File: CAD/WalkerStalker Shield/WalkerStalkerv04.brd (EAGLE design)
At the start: 49.5 x 53.3 mm, 25 parts

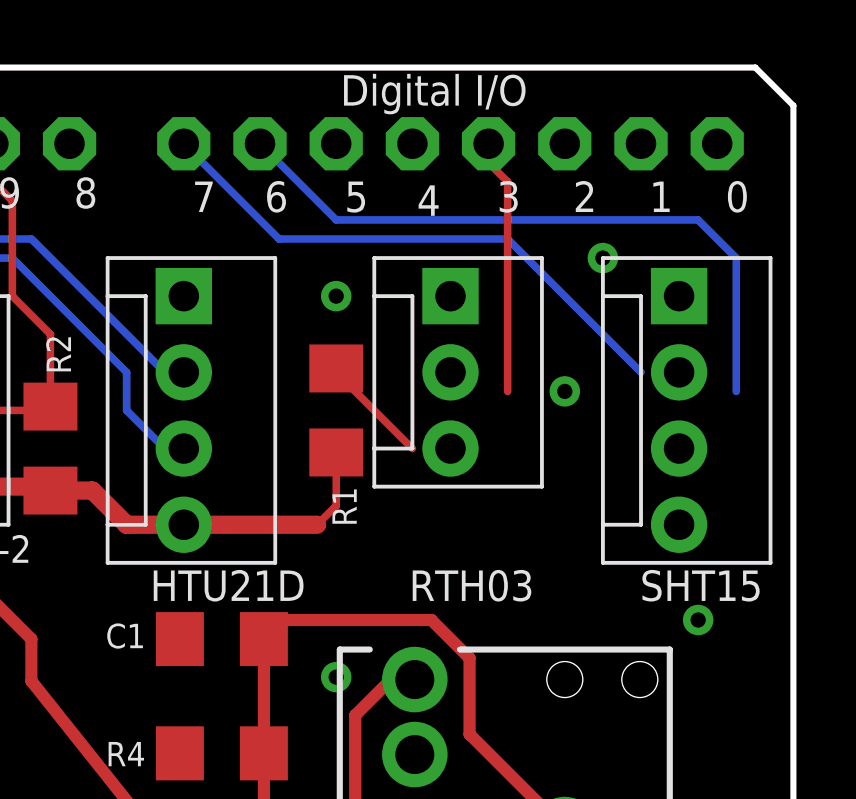
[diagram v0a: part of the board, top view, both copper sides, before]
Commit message: Fixed Temperature sensors
+ Temperature sensors are now called by explicit address, rather than
index, which was not consistent (could not tell if sensor was wall or
air)
+ Unit IDs are not transmitted in data packets for easy identification
+Mounting bracket for TMP006 sensor added (3D file)
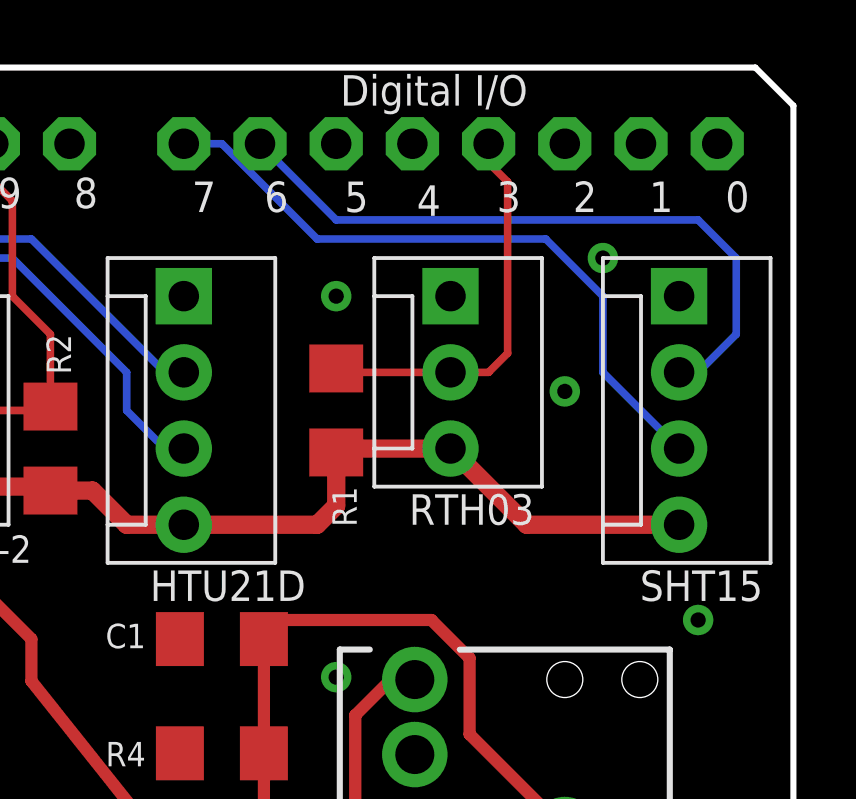
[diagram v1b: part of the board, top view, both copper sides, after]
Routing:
- net +3V3: track 119.1 -> 132.4 mm
- net SHT15-CL: track 18.4 -> 22.2 mm
- net RHT03: track 12.2 -> 13.4 mm
- net SHT15-DA: track 21.9 -> 22.4 mm
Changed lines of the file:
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@@
 <layer number="23" name="tOrigins" color="15" fill="1" visible="yes" active="yes"/>
 <layer number="24" name="bOrigins" color="15" fill="1" visible="yes" active="yes"/>
-<layer number="25" name="tNames" color="7" fill="1" visible="no" active="yes"/>
+<layer number="25" name="tNames" color="7" fill="1" visible="yes" active="yes"/>
 <layer number="26" name="bNames" color="7" fill="1" visible="no" active="yes"/>
-<layer number="27" name="tValues" color="7" fill="1" visible="no" active="yes"/>
+<layer number="27" name="tValues" color="7" fill="1" visible="yes" active="yes"/>
 <layer number="28" name="bValues" color="7" fill="1" visible="no" active="yes"/>
 <layer number="29" name="tStop" color="7" fill="3" visible="no" active="yes"/>
@@
 <text x="2.54" y="38.1" size="1.016" layer="25" font="vector" ratio="15" rot="R90">TMP006</text>
 <text x="33.274" y="36.576" size="1.016" layer="25" font="vector" ratio="15" rot="R180">HTU21D</text>
-<text x="40.894" y="36.576" size="1.016" layer="25" font="vector" ratio="15" rot="R180">RTH03</text>
+<text x="40.894" y="39.116" size="1.016" layer="25" font="vector" ratio="15" rot="R180">RTH03</text>
 <text x="48.514" y="36.576" size="1.016" layer="25" font="vector" ratio="15" rot="R180">SHT15</text>
 <text x="6.604" y="11.176" size="1.016" layer="25" font="vector" ratio="15" rot="R180">BH1750</text>
@@
 <via x="34.29" y="33.02" extent="1-16" drill="0.508"/>
 <contactref element="RHT1" pad="1"/>
-<wire x1="43.18" y1="46.99" x2="45.72" y2="45.72" width="0" layer="19" extent="1-1"/>
-<wire x1="41.91" y1="42.545" x2="43.18" y2="46.99" width="0" layer="19" extent="1-1"/>
-<wire x1="38.1" y1="45.72" x2="41.91" y2="42.545" width="0" layer="19" extent="1-1"/>
-<wire x1="34.29" y1="45.72" x2="38.1" y2="45.72" width="0" layer="19" extent="1-1"/>
-<wire x1="29.21" y1="45.72" x2="34.29" y2="45.72" width="0" layer="19" extent="1-1"/>
-<wire x1="46.355" y1="34.925" x2="41.91" y2="42.545" width="0" layer="19" extent="1-1"/>
-<wire x1="20.32" y1="44.45" x2="29.21" y2="45.72" width="0" layer="19" extent="1-1"/>
-<wire x1="16.51" y1="40.64" x2="20.32" y2="44.45" width="0" layer="19" extent="1-1"/>
-<wire x1="12.7" y1="44.45" x2="16.51" y2="40.64" width="0" layer="19" extent="1-1"/>
-<wire x1="10.16" y1="50.8" x2="12.7" y2="44.45" width="0" layer="19" extent="1-1"/>
-<wire x1="3.81" y1="48.26" x2="10.16" y2="50.8" width="0" layer="19" extent="1-1"/>
-<wire x1="5.08" y1="44.45" x2="3.81" y2="48.26" width="0" layer="19" extent="1-1"/>
-<wire x1="11.43" y1="35.56" x2="16.51" y2="40.64" width="0" layer="19" extent="1-1"/>
-<wire x1="11.43" y1="27.94" x2="11.43" y2="35.56" width="0" layer="19" extent="1-1"/>
-<wire x1="7.62" y1="23.495" x2="11.43" y2="27.94" width="0" layer="19" extent="1-1"/>
-<wire x1="7.62" y1="16.51" x2="7.62" y2="23.495" width="0" layer="19" extent="1-1"/>
-<wire x1="5.08" y1="12.7" x2="7.62" y2="16.51" width="0" layer="19" extent="1-1"/>
-<wire x1="11.43" y1="12.7" x2="7.62" y2="16.51" width="0" layer="19" extent="1-1"/>
-<wire x1="5.08" y1="31.115" x2="11.43" y2="27.94" width="0" layer="19" extent="1-1"/>
-<wire x1="20.32" y1="10.795" x2="11.43" y2="12.7" width="0" layer="19" extent="1-1"/>
-<wire x1="21.72" y1="14.605" x2="20.32" y2="10.795" width="0" layer="19" extent="1-1"/>
-<wire x1="24.13" y1="2.54" x2="20.32" y2="10.795" width="0" layer="19" extent="1-1"/>
-<wire x1="26.67" y1="2.54" x2="24.13" y2="2.54" width="0" layer="19" extent="1-1"/>
-<wire x1="7.62" y1="3.175" x2="5.08" y2="12.7" width="0" layer="19" extent="1-1"/>
-<wire x1="32.385" y1="18.415" x2="21.72" y2="14.605" width="0" layer="19" extent="1-1"/>
-<wire x1="29.08" y1="34.29" x2="29.21" y2="45.72" width="0" layer="19" extent="1-1"/>
-<wire x1="29.08" y1="30.48" x2="29.08" y2="34.29" width="0" layer="19" extent="1-1"/>
-<wire x1="34.29" y1="33.02" x2="29.08" y2="34.29" width="0" layer="19" extent="1-1"/>
-<wire x1="24.13" y1="27.94" x2="29.08" y2="30.48" width="0" layer="19" extent="1-1"/>
-<wire x1="43.18" y1="10.16" x2="32.385" y2="18.415" width="0" layer="19" extent="1-1"/>
-<wire x1="46.355" y1="18.415" x2="43.18" y2="10.16" width="0" layer="19" extent="1-1"/>
 </signal>
 <signal name="RESET">
@@
 <contactref element="R1" pad="2"/>
 <wire x1="19.05" y1="5.715" x2="19.05" y2="8.89" width="0.6096" layer="1"/>
-<wire x1="34.29" y1="40.51" x2="34.29" y2="38.735" width="0.254" layer="1"/>
-<wire x1="34.29" y1="38.735" x2="33.655" y2="38.1" width="0.254" layer="1"/>
+<wire x1="34.29" y1="40.51" x2="34.29" y2="38.735" width="0.6096" layer="1"/>
+<wire x1="34.29" y1="38.735" x2="33.655" y2="38.1" width="0.6096" layer="1"/>
 <wire x1="24.764515625" y1="39.238625" x2="26.166375" y2="39.238625" width="0.6096" layer="1"/>
 <wire x1="26.166375" y1="39.238625" x2="27.305" y2="38.1" width="0.6096" layer="1"/>
@@
 <wire x1="19.05" y1="20.32" x2="11.43" y2="20.32" width="0.6096" layer="16"/>
 <contactref element="RHT1" pad="3"/>
-<wire x1="38.1" y1="40.64" x2="45.72" y2="38.1" width="0" layer="19" extent="1-1"/>
-<wire x1="34.29" y1="40.51" x2="38.1" y2="40.64" width="0" layer="19" extent="1-1"/>
+<wire x1="45.72" y1="38.1" x2="40.64" y2="38.1" width="0.6096" layer="1"/>
+<wire x1="40.64" y1="38.1" x2="38.1" y2="40.64" width="0.6096" layer="1"/>
+<wire x1="34.29" y1="40.51" x2="35.055" y2="40.51" width="0.254" layer="1"/>
+<wire x1="38.1" y1="40.64" x2="34.42" y2="40.64" width="0.6096" layer="1"/>
+<wire x1="34.42" y1="40.64" x2="34.29" y2="40.51" width="0.254" layer="1"/>
 </signal>
 <signal name="TEMP_DQ">
@@
 <signal name="RHT03">
 <contactref element="JP-DIGITAL1" pad="4"/>
-<wire x1="40.005" y1="42.545" x2="40.005" y2="49.53" width="0.254" layer="1"/>
 <wire x1="40.005" y1="49.53" x2="39.37" y2="50.165" width="0.254" layer="1"/>
 <wire x1="39.37" y1="50.165" x2="39.37" y2="50.8" width="0.254" layer="1"/>
 <contactref element="R1" pad="1"/>
 <wire x1="34.29" y1="43.31" x2="34.29" y2="43.18" width="0.254" layer="1"/>
-<wire x1="34.29" y1="43.18" x2="36.83" y2="40.64" width="0.254" layer="1"/>
 <contactref element="RHT1" pad="2"/>
-<wire x1="40.005" y1="42.545" x2="38.1" y2="43.18" width="0" layer="19" extent="1-1"/>
-<wire x1="36.83" y1="40.64" x2="38.1" y2="43.18" width="0" layer="19" extent="1-1"/>
+<wire x1="34.29" y1="43.18" x2="38.1" y2="43.18" width="0.254" layer="1"/>
+<wire x1="38.1" y1="43.18" x2="39.37" y2="43.18" width="0.254" layer="1"/>
+<wire x1="39.37" y1="43.18" x2="40.005" y2="43.815" width="0.254" layer="1"/>
+<wire x1="40.005" y1="43.815" x2="40.005" y2="49.53" width="0.254" layer="1"/>
 </signal>
 <signal name="SHT15-DA">
-<wire x1="47.625" y1="42.545" x2="47.625" y2="46.99" width="0.254" layer="16"/>
 <wire x1="47.625" y1="46.99" x2="46.355" y2="48.26" width="0.254" layer="16"/>
 <wire x1="46.355" y1="48.26" x2="34.29" y2="48.26" width="0.254" layer="16"/>
@@
 <wire x1="31.75" y1="50.8" x2="34.29" y2="48.26" width="0.254" layer="16"/>
 <contactref element="SHT1" pad="2"/>
-<wire x1="47.625" y1="42.545" x2="45.72" y2="43.18" width="0" layer="19" extent="16-16"/>
+<wire x1="45.72" y1="43.18" x2="46.355" y2="43.18" width="0.254" layer="16"/>
+<wire x1="46.355" y1="43.18" x2="47.625" y2="44.45" width="0.254" layer="16"/>
+<wire x1="47.625" y1="44.45" x2="47.625" y2="46.99" width="0.254" layer="16"/>
 </signal>
 <signal name="SHT15-CL">
-<wire x1="40.005" y1="47.625" x2="44.45" y2="43.18" width="0.254" layer="16"/>
-<wire x1="40.005" y1="47.625" x2="32.385" y2="47.625" width="0.254" layer="16"/>
 <contactref element="JP-DIGITAL1" pad="8"/>
-<wire x1="29.21" y1="50.8" x2="32.385" y2="47.625" width="0.254" layer="16"/>
 <contactref element="SHT1" pad="3"/>
-<wire x1="44.45" y1="43.18" x2="45.72" y2="40.64" width="0" layer="19" extent="16-16"/>
+<wire x1="29.21" y1="50.8" x2="30.48" y2="50.8" width="0.254" layer="16"/>
+<wire x1="30.48" y1="50.8" x2="33.655" y2="47.625" width="0.254" layer="16"/>
+<wire x1="33.655" y1="47.625" x2="41.275" y2="47.625" width="0.254" layer="16"/>
+<wire x1="41.275" y1="47.625" x2="43.18" y2="45.72" width="0.254" layer="16"/>
+<wire x1="43.18" y1="45.72" x2="43.18" y2="43.18" width="0.254" layer="16"/>
+<wire x1="43.18" y1="43.18" x2="45.72" y2="40.64" width="0.254" layer="16"/>
 </signal>
 <signal name="LDR">
